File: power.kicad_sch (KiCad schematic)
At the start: 40 parts, among them T1 net-tie, U2 TPS546D24ARVFR

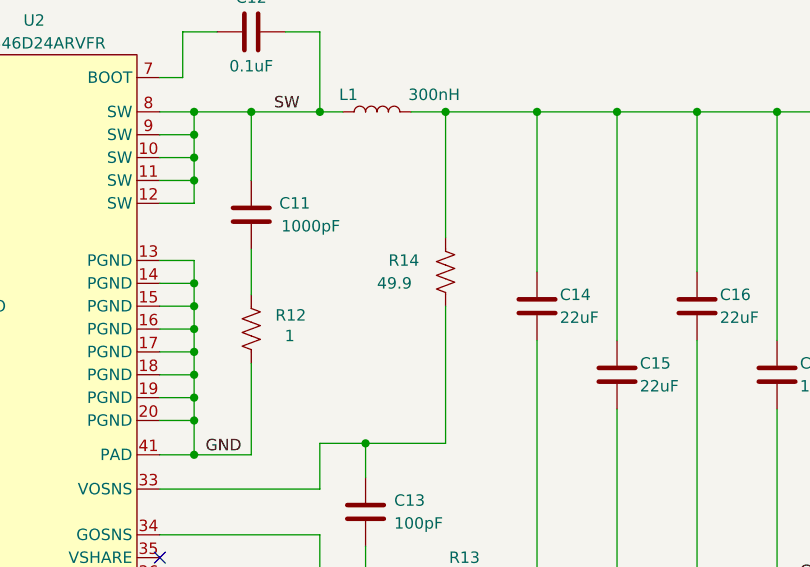
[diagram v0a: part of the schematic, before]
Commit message: switching to gamma/600 naming
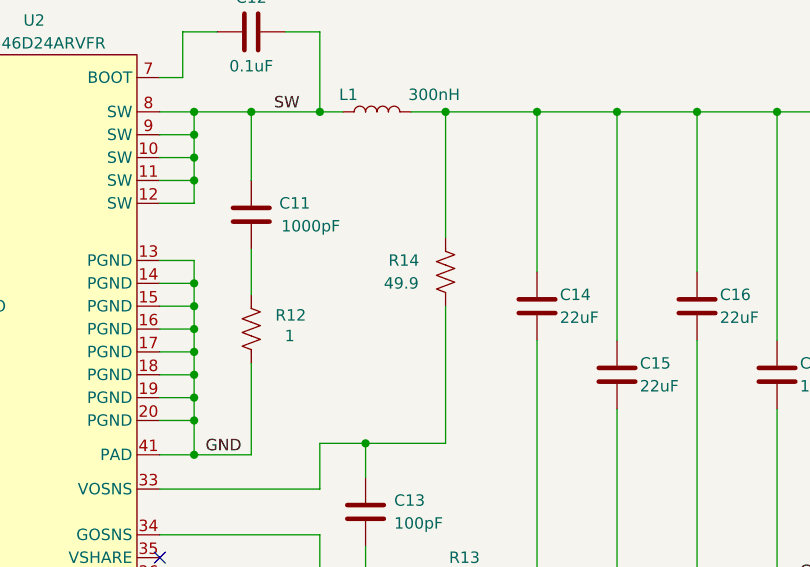
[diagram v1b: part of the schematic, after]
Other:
- title: bitaxeSupra -> bitaxeGamma
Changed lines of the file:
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@@
 	(paper "A")
 	(title_block
-		(title "bitaxeSupra")
-		(date "2024-04-07")
-		(rev "402")
+		(title "bitaxeGamma")
+		(date "2024-07-02")
+		(rev "600x")
 	)
 	(junction
@@
 		)
 		(instances
-			(project "bitaxeSupra"
+			(project "bitaxeGamma"
 				(path "/e63e39d7-6ac0-4ffd-8aa3-1841a4541b55/8ec0a9c6-2b78-44ef-a83d-9047d2828409"
 					(reference "C14")
@@
 		)
 		(instances
-			(project "bitaxeSupra"
+			(project "bitaxeGamma"
 				(path "/e63e39d7-6ac0-4ffd-8aa3-1841a4541b55/8ec0a9c6-2b78-44ef-a83d-9047d2828409"
 					(reference "C2")
@@
 		)
 		(property "Value" "49.9"
-			(at 160.02 58.42 0)
+			(at 160.782 58.42 0)
 			(effects
 				(font
@@
 		)
 		(instances
-			(project "bitaxeSupra"
+			(project "bitaxeGamma"
 				(path "/e63e39d7-6ac0-4ffd-8aa3-1841a4541b55/8ec0a9c6-2b78-44ef-a83d-9047d2828409"
 					(reference "R14")
@@
 		)
 		(instances
-			(project "bitaxeSupra"
+			(project "bitaxeGamma"
 				(path "/e63e39d7-6ac0-4ffd-8aa3-1841a4541b55/8ec0a9c6-2b78-44ef-a83d-9047d2828409"
 					(reference "C10")
@@
 		)
 		(instances
-			(project "bitaxeSupra"
+			(project "bitaxeGamma"
 				(path "/e63e39d7-6ac0-4ffd-8aa3-1841a4541b55/8ec0a9c6-2b78-44ef-a83d-9047d2828409"
 					(reference "TP4")
@@
 		)
 		(instances
-			(project "bitaxeSupra"
+			(project "bitaxeGamma"
 				(path "/e63e39d7-6ac0-4ffd-8aa3-1841a4541b55/8ec0a9c6-2b78-44ef-a83d-9047d2828409"
 					(reference "C1")
@@
 		)
 		(instances
-			(project "bitaxeSupra"
+			(project "bitaxeGamma"
 				(path "/e63e39d7-6ac0-4ffd-8aa3-1841a4541b55/8ec0a9c6-2b78-44ef-a83d-9047d2828409"
 					(reference "R8")
@@
 		)
 		(instances
-			(project "bitaxeSupra"
+			(project "bitaxeGamma"
 				(path "/e63e39d7-6ac0-4ffd-8aa3-1841a4541b55/8ec0a9c6-2b78-44ef-a83d-9047d2828409"
 					(reference "R10")
@@
 		)
 		(instances
-			(project "bitaxeSupra"
+			(project "bitaxeGamma"
 				(path "/e63e39d7-6ac0-4ffd-8aa3-1841a4541b55/8ec0a9c6-2b78-44ef-a83d-9047d2828409"
 					(reference "C13")
@@
 		)
 		(instances
-			(project "bitaxeSupra"
+			(project "bitaxeGamma"
 				(path "/e63e39d7-6ac0-4ffd-8aa3-1841a4541b55/8ec0a9c6-2b78-44ef-a83d-9047d2828409"
 					(reference "L1")
@@
 		)
 		(instances
-			(project "bitaxeSupra"
+			(project "bitaxeGamma"
 				(path "/e63e39d7-6ac0-4ffd-8aa3-1841a4541b55/8ec0a9c6-2b78-44ef-a83d-9047d2828409"
 					(reference "TP3")
@@
 		)
 		(instances
-			(project "bitaxeSupra"
+			(project "bitaxeGamma"
 				(path "/e63e39d7-6ac0-4ffd-8aa3-1841a4541b55/8ec0a9c6-2b78-44ef-a83d-9047d2828409"
 					(reference "C19")
@@
 		)
 		(instances
-			(project "bitaxeSupra"
+			(project "bitaxeGamma"
 				(path "/e63e39d7-6ac0-4ffd-8aa3-1841a4541b55/8ec0a9c6-2b78-44ef-a83d-9047d2828409"
 					(reference "C18")
@@
 		)
 		(instances
-			(project "bitaxeSupra"
+			(project "bitaxeGamma"
 				(path "/e63e39d7-6ac0-4ffd-8aa3-1841a4541b55/8ec0a9c6-2b78-44ef-a83d-9047d2828409"
 					(reference "C7")
@@
 		)
 		(instances
-			(project "bitaxeSupra"
+			(project "bitaxeGamma"
 				(path "/e63e39d7-6ac0-4ffd-8aa3-1841a4541b55/8ec0a9c6-2b78-44ef-a83d-9047d2828409"
 					(reference "U2")
@@
 		)
 		(instances
-			(project "bitaxeSupra"
+			(project "bitaxeGamma"
 				(path "/e63e39d7-6ac0-4ffd-8aa3-1841a4541b55/8ec0a9c6-2b78-44ef-a83d-9047d2828409"
 					(reference "C11")
@@
 		)
 		(instances
-			(project "bitaxeSupra"
+			(project "bitaxeGamma"
 				(path "/e63e39d7-6ac0-4ffd-8aa3-1841a4541b55/8ec0a9c6-2b78-44ef-a83d-9047d2828409"
 					(reference "C4")
@@
 		)
 		(instances
-			(project "bitaxeSupra"
+			(project "bitaxeGamma"
 				(path "/e63e39d7-6ac0-4ffd-8aa3-1841a4541b55/8ec0a9c6-2b78-44ef-a83d-9047d2828409"
 					(reference "R5")
@@
 		)
 		(instances
-			(project "bitaxeSupra"
+			(project "bitaxeGamma"
 				(path "/e63e39d7-6ac0-4ffd-8aa3-1841a4541b55/8ec0a9c6-2b78-44ef-a83d-9047d2828409"
 					(reference "C3")
@@
 		)
 		(instances
-			(project "bitaxeSupra"
+			(project "bitaxeGamma"
 				(path "/e63e39d7-6ac0-4ffd-8aa3-1841a4541b55/8ec0a9c6-2b78-44ef-a83d-9047d2828409"
 					(reference "R6")
@@
 		)
 		(instances
-			(project "bitaxeSupra"
+			(project "bitaxeGamma"
 				(path "/e63e39d7-6ac0-4ffd-8aa3-1841a4541b55/8ec0a9c6-2b78-44ef-a83d-9047d2828409"
 					(reference "R3")
@@
 		)
 		(instances
-			(project "bitaxeSupra"
+			(project "bitaxeGamma"
 				(path "/e63e39d7-6ac0-4ffd-8aa3-1841a4541b55/8ec0a9c6-2b78-44ef-a83d-9047d2828409"
 					(reference "C20")
@@
 		)
 		(instances
-			(project "bitaxeSupra"
+			(project "bitaxeGamma"
 				(path "/e63e39d7-6ac0-4ffd-8aa3-1841a4541b55/8ec0a9c6-2b78-44ef-a83d-9047d2828409"
 					(reference "R1")
@@
 		)
 		(instances
-			(project "bitaxeSupra"
+			(project "bitaxeGamma"
 				(path "/e63e39d7-6ac0-4ffd-8aa3-1841a4541b55/8ec0a9c6-2b78-44ef-a83d-9047d2828409"
 					(reference "T1")
@@
 		)
 		(instances
-			(project "bitaxeSupra"
+			(project "bitaxeGamma"
 				(path "/e63e39d7-6ac0-4ffd-8aa3-1841a4541b55/8ec0a9c6-2b78-44ef-a83d-9047d2828409"
 					(reference "C12")
@@
 		)
 		(instances
-			(project "bitaxeSupra"
+			(project "bitaxeGamma"
 				(path "/e63e39d7-6ac0-4ffd-8aa3-1841a4541b55/8ec0a9c6-2b78-44ef-a83d-9047d2828409"
 					(reference "R11")
@@
 		)
 		(instances
-			(project "bitaxeSupra"
+			(project "bitaxeGamma"
 				(path "/e63e39d7-6ac0-4ffd-8aa3-1841a4541b55/8ec0a9c6-2b78-44ef-a83d-9047d2828409"
 					(reference "R15")
@@
 		)
 		(instances
-			(project "bitaxeSupra"
+			(project "bitaxeGamma"
 				(path "/e63e39d7-6ac0-4ffd-8aa3-1841a4541b55/8ec0a9c6-2b78-44ef-a83d-9047d2828409"
 					(reference "C5")
@@
 		)
 		(instances
-			(project "bitaxeSupra"
+			(project "bitaxeGamma"
 				(path "/e63e39d7-6ac0-4ffd-8aa3-1841a4541b55/8ec0a9c6-2b78-44ef-a83d-9047d2828409"
 					(reference "C8")
@@
 		)
 		(instances
-			(project "bitaxeSupra"
+			(project "bitaxeGamma"
 				(path "/e63e39d7-6ac0-4ffd-8aa3-1841a4541b55/8ec0a9c6-2b78-44ef-a83d-9047d2828409"
 					(reference "C6")
@@
 		)
 		(instances
-			(project "bitaxeSupra"
+			(project "bitaxeGamma"
 				(path "/e63e39d7-6ac0-4ffd-8aa3-1841a4541b55/8ec0a9c6-2b78-44ef-a83d-9047d2828409"
 					(reference "C9")
@@
 		)
 		(instances
-			(project "bitaxeSupra"
+			(project "bitaxeGamma"
 				(path "/e63e39d7-6ac0-4ffd-8aa3-1841a4541b55/8ec0a9c6-2b78-44ef-a83d-9047d2828409"
 					(reference "R2")
@@
 		)
 		(instances
-			(project "bitaxeSupra"
+			(project "bitaxeGamma"
 				(path "/e63e39d7-6ac0-4ffd-8aa3-1841a4541b55/8ec0a9c6-2b78-44ef-a83d-9047d2828409"
 					(reference "C15")
@@
 		)
 		(instances
-			(project "bitaxeSupra"
+			(project "bitaxeGamma"
 				(path "/e63e39d7-6ac0-4ffd-8aa3-1841a4541b55/8ec0a9c6-2b78-44ef-a83d-9047d2828409"
 					(reference "R7")
@@
 		)
 		(instances
-			(project "bitaxeSupra"
+			(project "bitaxeGamma"
 				(path "/e63e39d7-6ac0-4ffd-8aa3-1841a4541b55/8ec0a9c6-2b78-44ef-a83d-9047d2828409"
 					(reference "C16")
@@
 		)
 		(instances
-			(project "bitaxeSupra"
+			(project "bitaxeGamma"
 				(path "/e63e39d7-6ac0-4ffd-8aa3-1841a4541b55/8ec0a9c6-2b78-44ef-a83d-9047d2828409"
 					(reference "C17")
@@
 		)
 		(instances
-			(project "bitaxeSupra"
+			(project "bitaxeGamma"
 				(path "/e63e39d7-6ac0-4ffd-8aa3-1841a4541b55/8ec0a9c6-2b78-44ef-a83d-9047d2828409"
 					(reference "R12")
@@
 		)
 		(instances
-			(project "bitaxeSupra"
+			(project "bitaxeGamma"
 				(path "/e63e39d7-6ac0-4ffd-8aa3-1841a4541b55/8ec0a9c6-2b78-44ef-a83d-9047d2828409"
 					(reference "R13")
@@
 		)
 		(instances
-			(project "bitaxeSupra"
+			(project "bitaxeGamma"
 				(path "/e63e39d7-6ac0-4ffd-8aa3-1841a4541b55/8ec0a9c6-2b78-44ef-a83d-9047d2828409"
 					(reference "R4")
@@
 		)
 		(instances
-			(project "bitaxeSupra"
+			(project "bitaxeGamma"
 				(path "/e63e39d7-6ac0-4ffd-8aa3-1841a4541b55/8ec0a9c6-2b78-44ef-a83d-9047d2828409"
 					(reference "R9")
@@
 		)
 	)
+	(sheet_instances
+		(path "/"
+			(page "1")
+		)
+	)
